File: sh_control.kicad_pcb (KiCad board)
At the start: 4 copper layers, 86.4 x 94.7 mm, 90 parts, among them IC1 SN75240PW, IC2 LM317MDCY, IC3 TPS73533DRBT, IC4 TLV76733DGNR, IC5 TUSB2046IBVF, IC6 TPS2044BDR, IC7 SN75240PW, J1 USB_B_Micro, J2 10129381-906001BLF, J3 10129381-906001BLF, Y1 6MHz

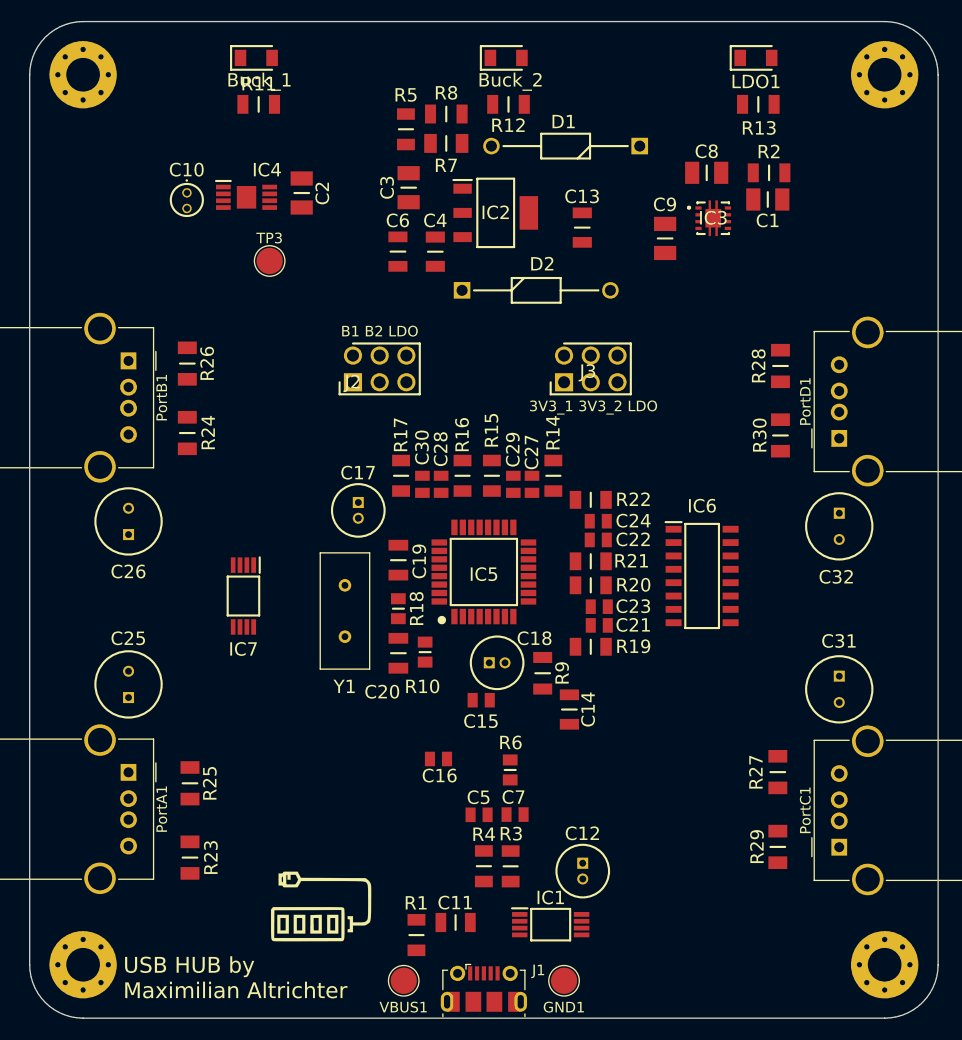
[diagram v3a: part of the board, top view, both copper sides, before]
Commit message: finished hub, added reste button
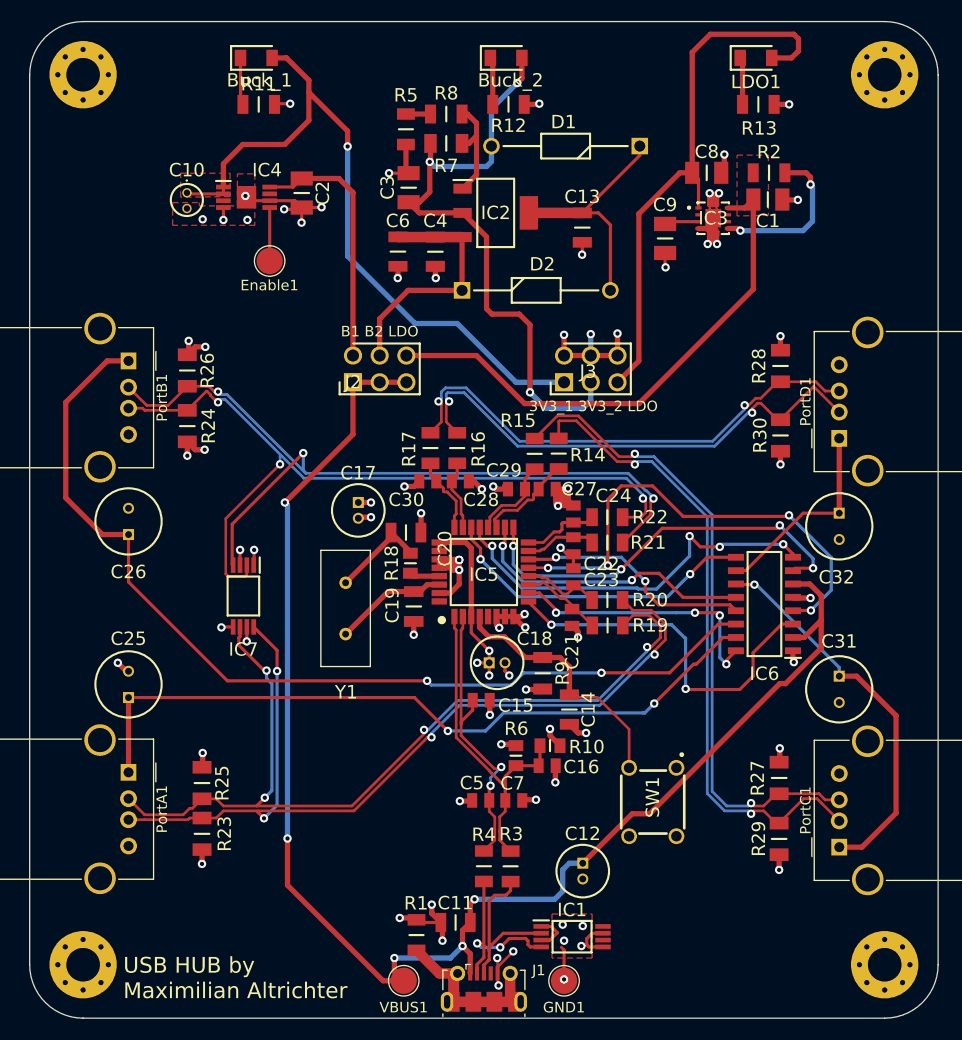
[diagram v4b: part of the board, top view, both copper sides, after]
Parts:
- removed G***: LOGO, logo_hub:logo
- added SW1: Reset, SamacSys_Parts:FSM4JH, F.Cu at (171.0, 107.5)
- moved R10 14.8 mm to (161.2, 102.1), turned to 180 degrees
- moved C20 11.5 mm to (147.5, 81.9), turned to 0 degrees
- moved C16 10.4 mm to (161.0, 104.0), turned to 0 degrees
- moved IC6 6.50 mm to (181.6, 88.6), turned to 180 degrees
- moved Y1 4.64 mm to (141.8, 91.5), turned to 90 degrees
- moved C19 4.64 mm to (148.3, 88.9), turned to 270 degrees
- moved R15 4.57 mm to (159.8, 74.4)
- moved R18 4.47 mm to (148.0, 84.8), turned to 90 degrees
- moved R17 3.84 mm to (149.9, 73.8)
- moved C23 3.76 mm to (163.4, 86.1), turned to 90 degrees
- moved C21 2.70 mm to (163.3, 89.9), turned to 270 degrees
- moved R16 2.68 mm to (152.4, 73.8)
- moved R19 2.59 mm to (166.7, 90.7)
- moved R23 2.53 mm to (128.1, 110.5), turned to 90 degrees
- moved C24 2.46 mm to (163.4, 80.1), turned to 90 degrees
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- renumbered TP3 to Enable1
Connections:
- net DM1 renamed D1-
- net DM2 renamed D2-
- net DM3 renamed D3-
- net DM4 renamed D4-
- net DMO renamed D0-
- net DM_downstream1 renamed D_DS_1_-
- net DM_downstream2 renamed D_DS_2_-
- net DM_downstream3 renamed D_DS_3_-
- net DM_downstream4 renamed D_DS_4_-
- net DP0 renamed D0+
- net DP1 renamed D1+
- net DP2 renamed D2+
- net DP3 renamed D3+
- net DP4 renamed D4+
- net DP_downstream1 renamed D_DS_1_+
- net DP_downstream2 renamed D_DS_2_+
- net DP_downstream3 renamed D_DS_3_+
- net DP_downstream4 renamed D_DS_4_+
- PortD1 pad 5: Net-(PortD1-Pad5) -> GND
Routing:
- net GND: track 0.00 -> 151.4 mm, vias 0 -> 71
- net VBUS: track 0.00 -> 143.3 mm, vias 0 -> 5
- net OUT2: track 0.00 -> 92.8 mm, vias 0 -> 2
- net D_DS_1_+: track 0.00 -> 85.6 mm, vias 0 -> 4
- net D_DS_1_-: track 0.00 -> 83.8 mm, vias 0 -> 4
- net D_DS_2_-: track 0.00 -> 76.7 mm, vias 0 -> 3
- net D_DS_2_+: track 0.00 -> 74.8 mm, vias 0 -> 3
- net OUT1: track 0.00 -> 69.8 mm, vias 0 -> 2
- net 3V3_Buck_1: track 0.00 -> 67.0 mm, vias 0 -> 1
- net D_DS_3_-: track 0.00 -> 61.8 mm, vias 0 -> 2
- net D_DS_3_+: track 0.00 -> 61.8 mm, vias 0 -> 2
- net 3V3_Buck_2: track 0.00 -> 59.6 mm, vias 0 -> 3
- net 3V3_LDO: track 0.00 -> 53.5 mm
- net LDO: track 0.00 -> 50.6 mm
- net D_DS_4_-: track 0.00 -> 48.7 mm, vias 0 -> 2
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- added copper zone on F.Cu, net 3V3_Buck_1
- added copper zone on F.Cu, net GND
- added copper zone on In1.Cu, net GND
- added copper zone on F.Cu, net LDO
- added copper zone on In2.Cu, net VCC

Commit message: review passed, bom created
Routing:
- net 3V3_LDO: track 53.5 -> 46.4 mm, vias 0 -> 2
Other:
- board text added: "USB HUB v3.2-EB by Maximilian Altrichter"
- board text removed: "USB HUB by Maximilian Altrichter"
